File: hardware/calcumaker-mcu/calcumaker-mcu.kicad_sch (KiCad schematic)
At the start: 0 parts

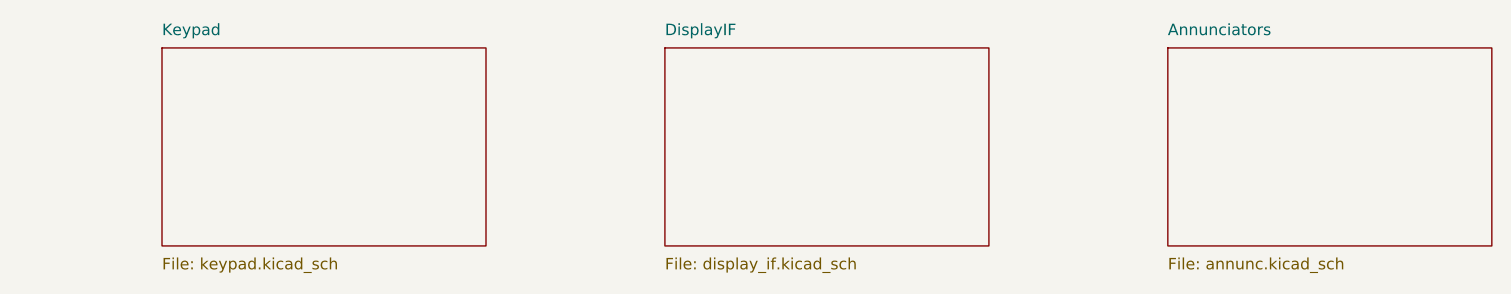
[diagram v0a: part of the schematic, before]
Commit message: hardware: 3-board split (MCU + keyboard + display), wired display, real connectors
Split the single logic board into three, wire the display as a KiCad
multi-channel design, and settle every interconnect on real, in-stock parts.

Three-board split (was two):
- Rename calcumaker-main -> calcumaker-mcu (brain/PSU logic board).
- New calcumaker-keyboard board: 50-key Cherry MX matrix + its own
  STM32G031K8U6 scanner (LCSC C432207, UFQFPN-32) + annunciator LEDs,
  mezzanine-stacked above the MCU board. Keyscanning is off the main board;
  only an I2C + UART link + KB_IRQ wake + power cross the mezzanine.

Display board (calcumaker-display):
- Corrected FJ5161AH to a SINGLE-digit 0.56" common-cathode part (C8093) --
  it is NOT a 4-digit module; 48 single digits (16/row x 3), authored symbol
  + 0.56" LTS6760 land. The old 4-digit CC56-12 mapping (and its 3D model)
  was the phantom "clock colon".
- Rebuilt as a KiCad multi-channel design: one reusable display_row.kicad_sch
  (1 TM1640 + 16 digits, fully wired) instantiated x3. Extended kschgen.py
  with wiring primitives + reused-sheet (multi-channel) support.

Connectors (real, verified LCSC / DigiKey parts):
- Display link -> 0.5mm 12P FFC: AFC01-S12FCA-00 (LCSC C262661) on both
  boards; cable = GCT FFC05-TIN 05-12-A-<len>-A-4-06-4-T (DigiKey accessory,
  length TBD). +5V/GND conductors doubled for the display LED current.
- Keyboard mezzanine -> low-profile Hirose DF40 (0.4mm, 2x5, 1.5mm stack):
  DF40C-10DS (C424636) + DF40C-10DP (C424635) -- dedicated KiCad footprint
  + 3D model, unlike the datasheet-less generic parts first considered.

Low-power & wake documented (two Stop domains; keypress -> G0 EXTI wake ->
KB_IRQ -> U575 WKUP; G0 also wakes on I2C address-match). calcumaker-core
is unchanged -- App still consumes (row,col).

All three boards generate + pass the structure check (mcu 52 / keyboard 119 /
display 60 components, all footprints assigned, no duplicate refs). Docs
(DESIGN.md, PARTS.md incl. a Non-B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
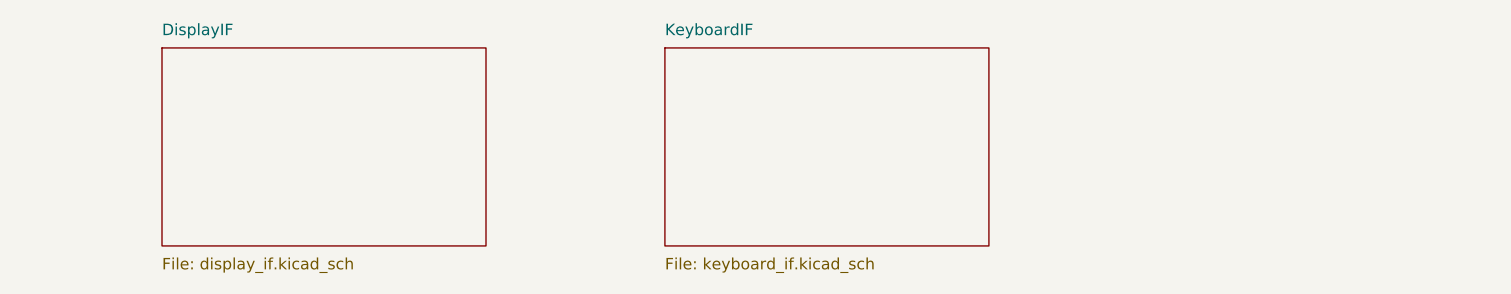
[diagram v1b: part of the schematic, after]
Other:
- removed sheet Annunciators
- removed sheet Keypad
- added sheet KeyboardIF (keyboard_if.kicad_sch)
- title: Calcumaker 16 — Main -> Calcumaker 16 — MCU
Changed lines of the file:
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@@
 	(paper "A3")
 	(title_block
-		(title "Calcumaker 16 — Main")
-		(date "2026-06-21")
-		(rev "0.1")
+		(title "Calcumaker 16 — MCU")
+		(date "2026-07-05")
+		(rev "0.2")
 		(company "calcumaker authors")
 		(comment 1 "Programmer's/technical arbitrary-precision RPN calculator")
-		(comment 2 "Main board: MCU + PSU + keypad + display interconnect (DRAFT)")
+		(comment 2 "MCU board: MCU + PSU + clock + SWD + display-IF + keyboard mezzanine (DRAFT)")
 	)
 	(sheet
@@
 		(stroke (width 0.1524) (type solid))
 		(fill (color 0 0 0 0.0000))
-		(property "Sheetname" "Keypad"
+		(property "Sheetname" "DisplayIF"
 			(at 264.16 39.37 0)
 			(effects (font (size 1.27 1.27)) (justify left bottom))
 		)
-		(property "Sheetfile" "keypad.kicad_sch"
+		(property "Sheetfile" "display_if.kicad_sch"
 			(at 264.16 63.91 0)
 			(effects (font (size 1.27 1.27)) (justify left top))
@@
 		(stroke (width 0.1524) (type solid))
 		(fill (color 0 0 0 0.0000))
-		(property "Sheetname" "DisplayIF"
+		(property "Sheetname" "KeyboardIF"
 			(at 320.04 39.37 0)
 			(effects (font (size 1.27 1.27)) (justify left bottom))
 		)
-		(property "Sheetfile" "display_if.kicad_sch"
+		(property "Sheetfile" "keyboard_if.kicad_sch"
 			(at 320.04 63.91 0)
 			(effects (font (size 1.27 1.27)) (justify left top))
 		)
-	)
-	(sheet
-		(at 375.92 40.64)
-		(size 36.00 22.00)
-		(fields_autoplaced yes)
-		(stroke (width 0.1524) (type solid))
-		(fill (color 0 0 0 0.0000))
-		(property "Sheetname" "Annunciators"
-			(at 375.92 39.37 0)
-			(effects (font (size 1.27 1.27)) (justify left bottom))
-		)
-		(property "Sheetfile" "annunc.kicad_sch"
-			(at 375.92 63.91 0)
-			(effects (font (size 1.27 1.27)) (justify left top))
-		)

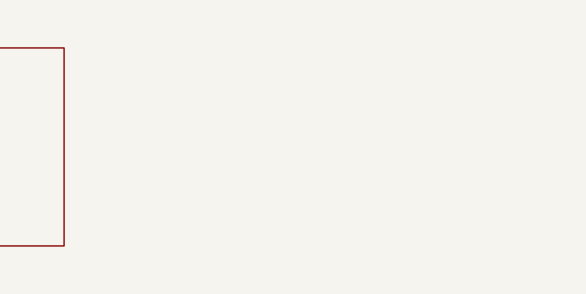
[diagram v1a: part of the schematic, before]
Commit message: hardware: MCU -> STM32U575RGT6 (LQFP-64) + 4MB QSPI flash; monospace wiring notes
MCU package + external flash
- Swap U1 STM32U575ZGT6 (LQFP-144) -> STM32U575RGT6 (LQFP-64, LCSC C5270980).
  The firmware links at ~323 KB so 1 MB flash is ample (~3x headroom), and with
  the key matrix scanned off-board the LQFP-64 has enough GPIO — smaller/cheaper.
- Correct the flash size everywhere: the STM32 `G` code = 1 MB (not 2 MB; the
  `I` parts are 2 MB). memory.x FLASH 2048K -> 1024K; .cargo runner -> RGTx.
- Add U7 W25Q32JVSSIQ, a 4 MB (32 Mbit) quad-SPI NOR (LCSC C179173, SOIC-8) on
  OCTOSPI1 as a new QSPIFlash sheet (+ R9 CS# pull-up + C26 decoupling) for
  memory-mapped (XIP) constants + state/program storage.
- mcu board 52 -> 55 components / 7 sheets. Docs (DESIGN.md, PARTS.md, READMEs,
  CLAUDE/AGENTS) updated; availability ladder now lists RGT6/VGT6/ZGT6.

Monospace, multi-line schematic wiring notes
- kschgen text_note() now renders notes in a monospace font (Courier New) so
  tables/columns line up; add note_block() + pin_table() helpers.
- Reformat all 14 per-sheet notes into titled, multi-line, aligned blocks —
  connector pinouts as PIN/SIGNAL tables, power/MCU sheets as wiring blocks.

The regenerated schematics carry both changes, so this is one commit. All three
boards regenerate + pass the structure check (mcu 55 / keyboard 119 / display
60, no duplicate refs).

Co-Authored-By: Claude Opus 4.8 (1M context) <noreply@anthropic.com>
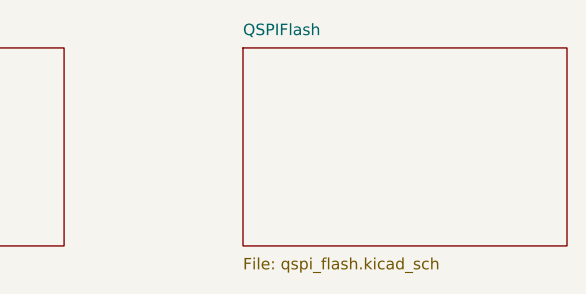
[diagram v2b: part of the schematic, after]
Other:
- added sheet QSPIFlash (qspi_flash.kicad_sch)
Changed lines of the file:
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@@
 	(title_block
 		(title "Calcumaker 16 — MCU")
-		(date "2026-07-05")
-		(rev "0.2")
+		(date "2026-07-06")
+		(rev "0.3")
 		(company "calcumaker authors")
 		(comment 1 "Programmer's/technical arbitrary-precision RPN calculator")
-		(comment 2 "MCU board: MCU + PSU + clock + SWD + display-IF + keyboard mezzanine (DRAFT)")
+		(comment 2 "MCU board: STM32U575RGT6 (LQFP-64) + PSU + clock + SWD + display-IF + keyboard mezzanine + 4MB QSPI flash (DRAFT)")
 	)
 	(sheet
@@
 			(effects (font (size 1.27 1.27)) (justify left top))
 		)
+	)
+	(sheet
+		(at 375.92 40.64)
+		(size 36.00 22.00)
+		(fields_autoplaced yes)
+		(stroke (width 0.1524) (type solid))
+		(fill (color 0 0 0 0.0000))
+		(property "Sheetname" "QSPIFlash"
+			(at 375.92 39.37 0)
+			(effects (font (size 1.27 1.27)) (justify left bottom))
+		)
+		(property "Sheetfile" "qspi_flash.kicad_sch"
+			(at 375.92 63.91 0)
+			(effects (font (size 1.27 1.27)) (justify left top))
+		)

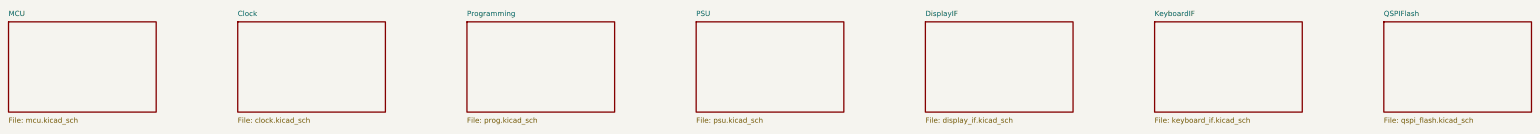
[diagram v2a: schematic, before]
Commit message: hw: assign the OCTOSPI1 pinout and fold Clock/Prog/DisplayIF into MCU
The MCU sheet carried a "verify OCTOSPI1 pin mapping is available on
LQFP-64" TODO and the flash sheet said to assign it "to the PB/PC bank".
Both are now settled, and the PB/PC hint was wrong.

On the U5 the OCTOSPI GPIOs belong to the OCTOSPI I/O manager, so the AF
signals are OCTOSPIM_P1_*/P2_*. LQFP-64 bonds out no Port-2 bus at all
(ports E/F/G absent; only P2_NCS is present), so Port 1 is mandatory —
and on Port 1 IO0..IO3 each have exactly one candidate pin. Only CLK
(PA3|PB10) and NCS (PA2|PA4|PC11) were a real choice:

  CLK PB10 AF10 p29   IO0 PB1 AF10 p27   IO2 PA7 AF10 p23
  NCS PA4  AF3  p20   IO1 PB0 AF10 p26   IO3 PA6 AF10 p22

PB10+PA4 keep the whole bus in a contiguous pin 20-29 cluster (short and
length-matchable for >=50 MHz quad) and leave PA2/PA3 whole as the USART2
TX/RX pair for the keyboard link. It costs SPI1_NSS and WKUP2, both of
which have alternates. Every pin is verified against ST's package-filtered
CubeMX pin database for STM32U575RGTx / LQFP-64.

Taking PA6/PA7 for the flash consumes SPI1_MISO/MOSI, so the display
module bus moves to SCK=PA5, MOSI=PB5, CS=PA15. No MISO is needed — the
12-pin FFC doesn't carry one.

Sheet surgery: Clock (Y1 + C24/C25), Programming (J4) and DisplayIF
(J3 + J7) were already merged into the MCU sheet, leaving three files
unreferenced from the root. Delete them. The notes were edited in place
rather than regenerated, so the manual eeschema wiring survives; the
structure check reports the same 46 components and the same ERC tally as
before the change.

Also fix two things DESIGN.md got wrong on the way past:
  - The Power Tree still showed a 5V boost gated by DISP_PWR_EN and a
    74HCT125 on the MCU board. Those parts live on the display module now
    (DESIGN.md says so elsewhere) and exist on no sheet here; the PSU has
    only the TPS63900. VSYS passes through raw to J3/J7.
  - The board is 46 components, not 55.

Still open: KB_IRQ 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
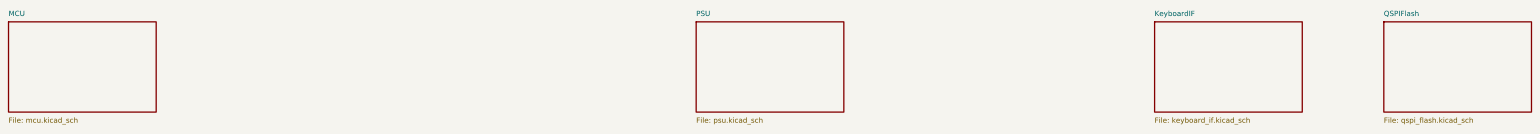
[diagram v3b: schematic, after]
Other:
- removed sheet Clock
- removed sheet DisplayIF
- removed sheet Programming
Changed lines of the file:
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@@
 	(generator "eeschema")
 	(generator_version "10.0")
-	(uuid "ca1c0000-0000-4000-8000-00000000ma01")
 	(paper "A3")
 	(title_block
@@
 	)
 	(sheet
+		(at 320.04 40.64)
+		(size 36 22)
+		(exclude_from_sim no)
+		(in_bom yes)
+		(on_board yes)
+		(dnp no)
+		(fields_autoplaced yes)
+		(stroke
+			(width 0.1524)
+			(type solid)
+		)
+		(fill
+			(color 0 0 0 0)
+		)
+		(property "Sheetname" "KeyboardIF"
+			(at 320.04 39.37 0)
+			(show_name no)
+			(do_not_autoplace no)
+			(effects
+				(font
+					(size 1.27 1.27)
+				)
+				(justify left bottom)
+			)
+		)
+		(property "Sheetfile" "keyboard_if.kicad_sch"
+			(at 320.04 63.91 0)
+			(show_name no)
+			(do_not_autoplace no)
+			(effects
+				(font
+					(size 1.27 1.27)
+				)
+				(justify left top)
+			)
+		)
+	)
+	(sheet
 		(at 40.64 40.64)
-		(size 36.00 22.00)
+		(size 36 22)
+		(exclude_from_sim no)
+		(in_bom yes)
+		(on_board yes)
+		(dnp no)
 		(fields_autoplaced yes)
-		(stroke (width 0.1524) (type solid))
-		(fill (color 0 0 0 0.0000))
+		(stroke
+			(width 0.1524)
+			(type solid)
+		)
+		(fill
+			(color 0 0 0 0)
+		)
 		(property "Sheetname" "MCU"
 			(at 40.64 39.37 0)
-			(effects (font (size 1.27 1.27)) (justify left bottom))
+			(show_name no)
+			(do_not_autoplace no)
+			(effects
+				(font
+					(size 1.27 1.27)
+				)
+				(justify left bottom)
+			)
 		)
 		(property "Sheetfile" "mcu.kicad_sch"
 			(at 40.64 63.91 0)
-			(effects (font (size 1.27 1.27)) (justify left top))
+			(show_name no)
+			(do_not_autoplace no)
+			(effects
+				(font
+					(size 1.27 1.27)
+				)
+				(justify left top)
+			)
 		)
 	)
 	(sheet
-		(at 96.52 40.64)
-		(size 36.00 22.00)
+		(at 375.92 40.64)
+		(size 36 22)
+		(exclude_from_sim no)
+		(in_bom yes)
+		(on_board yes)
+		(dnp no)
 		(fields_autoplaced yes)
-		(stroke (width 0.1524) (type solid))
-		(fill (color 0 0 0 0.0000))
-		(property "Sheetname" "Clock"
-			(at 96.52 39.37 0)
-			(effects (font (size 1.27 1.27)) (justify left bottom))
+		(stroke
+			(width 0.1524)
+			(type solid)
 		)
-		(property "Sheetfile" "clock.kicad_sch"
-			(at 96.52 63.91 0)
-			(effects (font (size 1.27 1.27)) (justify left top))
+		(fill
+			(color 0 0 0 0)
 		)
-	)
-	(sheet
-		(at 152.40 40.64)
-		(size 36.00 22.00)
-		(fields_autoplaced yes)
-		(stroke (width 0.1524) (type solid))
-		(fill (color 0 0 0 0.0000))
-		(property "Sheetname" "Programming"
-			(at 152.40 39.37 0)
-			(effects (font (size 1.27 1.27)) (justify left bottom))
+		(property "Sheetname" "QSPIFlash"
+			(at 375.92 39.37 0)
+			(show_name no)
+			(do_not_autoplace no)
+			(effects
+				(font
+					(size 1.27 1.27)
+				)
+				(justify left bottom)
+			)
 		)
-		(property "Sheetfile" "prog.kicad_sch"
-			(at 152.40 63.91 0)
-			(effects (font (size 1.27 1.27)) (justify left top))
+		(property "Sheetfile" "qspi_flash.kicad_sch"
+			(at 375.92 63.91 0)
+			(show_name no)
+			(do_not_autoplace no)
+			(effects
+				(font
+					(size 1.27 1.27)
+				)
+				(justify left top)
+			)
 		)
 	)
 	(sheet
 		(at 208.28 40.64)
-		(size 36.00 22.00)
+		(size 36 22)
+		(exclude_from_sim no)
+		(in_bom yes)
+		(on_board yes)
+		(dnp no)
 		(fields_autoplaced yes)
-		(stroke (width 0.1524) (type solid))
-		(fill (color 0 0 0 0.0000))
+		(stroke
+			(width 0.1524)
+			(type solid)
+		)
+		(fill
+			(color 0 0 0 0)
+		)
 		(property "Sheetname" "PSU"
 			(at 208.28 39.37 0)
-			(effects (font (size 1.27 1.27)) (justify left bottom))
+			(show_name no)
+			(do_not_autoplace no)
+			(effects
+				(font
+					(size 1.27 1.27)
+				)
+				(justify left bottom)
+			)
 		)
 		(property "Sheetfile" "psu.kicad_sch"
 			(at 208.28 63.91 0)
-			(effects (font (size 1.27 1.27)) (justify left top))
+			(show_name no)
+			(do_not_autoplace no)
+			(effects
+				(font
+					(size 1.27 1.27)
+				)
+				(justify left top)
+			)
 		)
 	)
-	(sheet
-		(at 264.16 40.64)
-		(size 36.00 22.00)
-		(fields_autoplaced yes)
-		(stroke (width 0.1524) (type solid))
-		(fill (color 0 0 0 0.0000))
-		(property "Sheetname" "DisplayIF"
-			(at 264.16 39.37 0)
-			(effects (font (size 1.27 1.27)) (justify left bottom))
-		)
-		(property "Sheetfile" "display_if.kicad_sch"
-			(at 264.16 63.91 0)
-			(effects (font (size 1.27 1.27)) (justify left top))
-		)
-	)
-	(sheet
-		(at 320.04 40.64)
-		(size 36.00 22.00)
-		(fields_autoplaced yes)
-		(stroke (width 0.1524) (type solid))
-		(fill (color 0 0 0 0.0000))
-		(property "Sheetname" "KeyboardIF"
-			(at 320.04 39.37 0)
-			(effects (font (size 1.27 1.27)) (justify left bottom))
-		)
-		(property "Sheetfile" "keyboard_if.kicad_sch"
-			(at 320.04 63.91 0)
-			(effects (font (size 1.27 1.27)) (justify left top))
-		)
-	)
-	(sheet
-		(at 375.92 40.64)
-		(size 36.00 22.00)
-		(fields_autoplaced yes)
-		(stroke (width 0.1524) (type solid))
-		(fill (color 0 0 0 0.0000))
-		(property "Sheetname" "QSPIFlash"
-			(at 375.92 39.37 0)
-			(effects (font (size 1.27 1.27)) (justify left bottom))
-		)
-		(property "Sheetfile" "qspi_flash.kicad_sch"
-			(at 375.92 63.91 0)
-			(effects (font (size 1.27 1.27)) (justify left top))
-		)
-	)
